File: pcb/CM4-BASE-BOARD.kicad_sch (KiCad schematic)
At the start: 17 parts, among them J1 THD-02-R, J2 Micro_SD_Card_Det2, J3 USB4105-GF-A, J4 PCIe-x1, U1 MagJack-A70-112-331N126, U2 TPD4EUSB30, U3 TPD4EUSB30, U5 RT9742AGJ5F

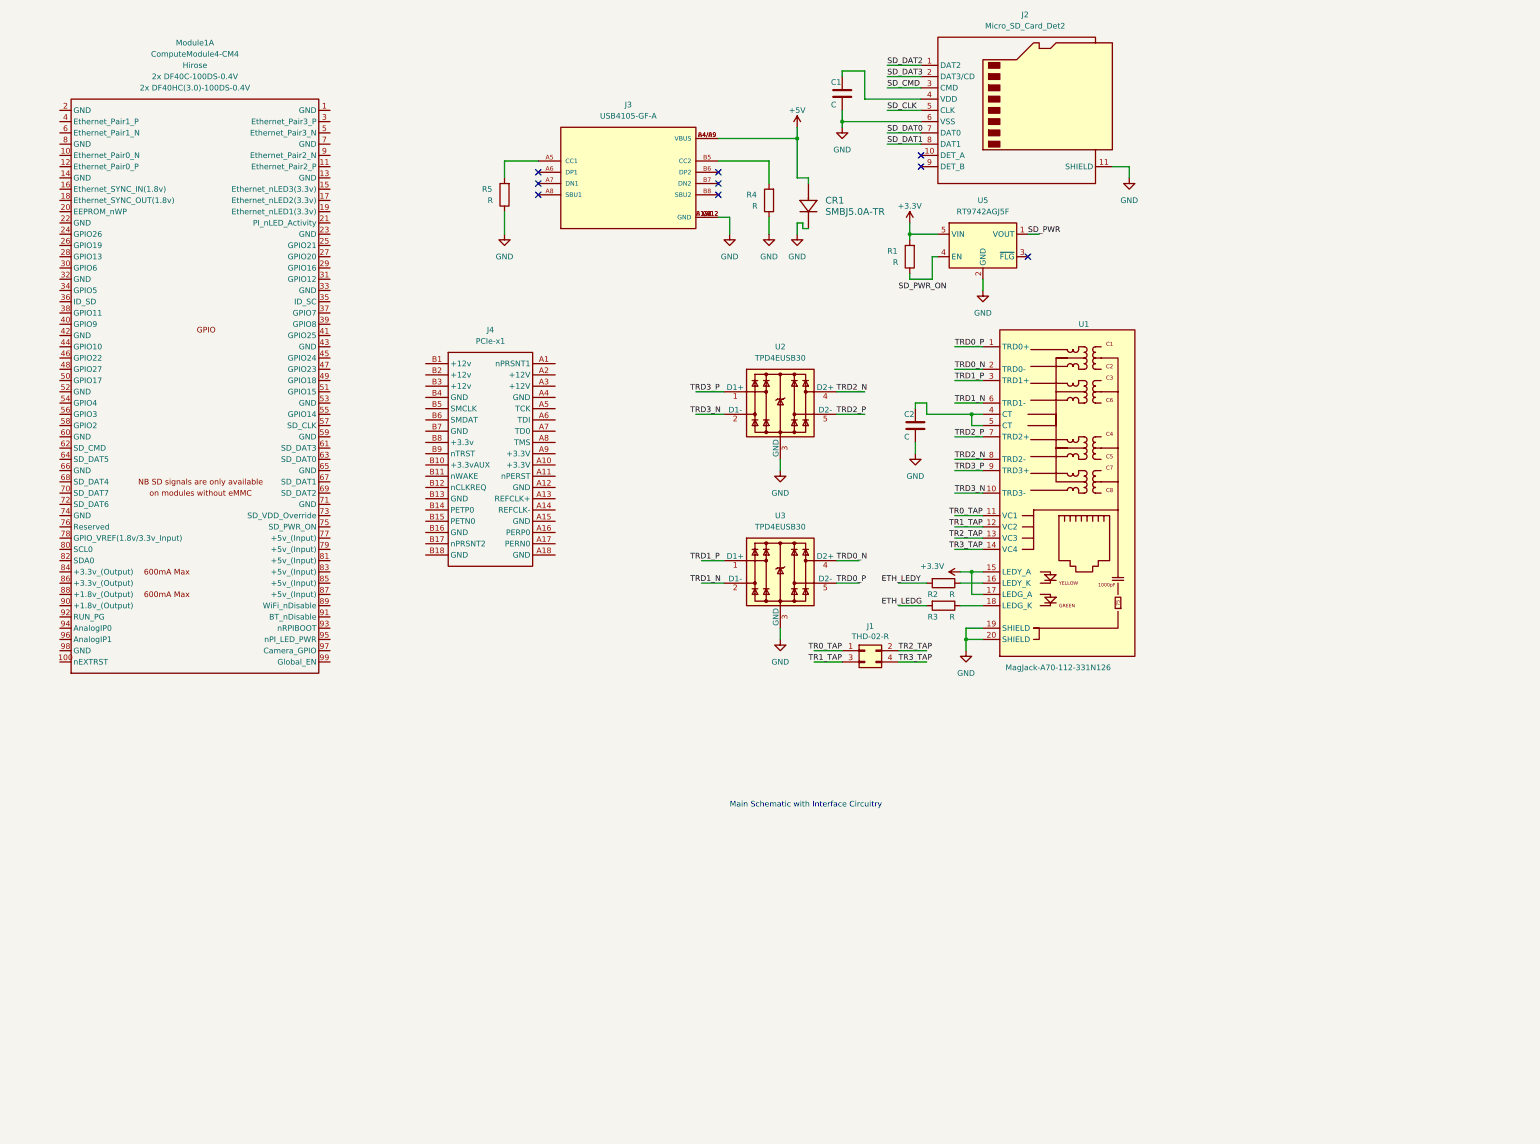
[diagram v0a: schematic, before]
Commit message: Added: concentrator and power section
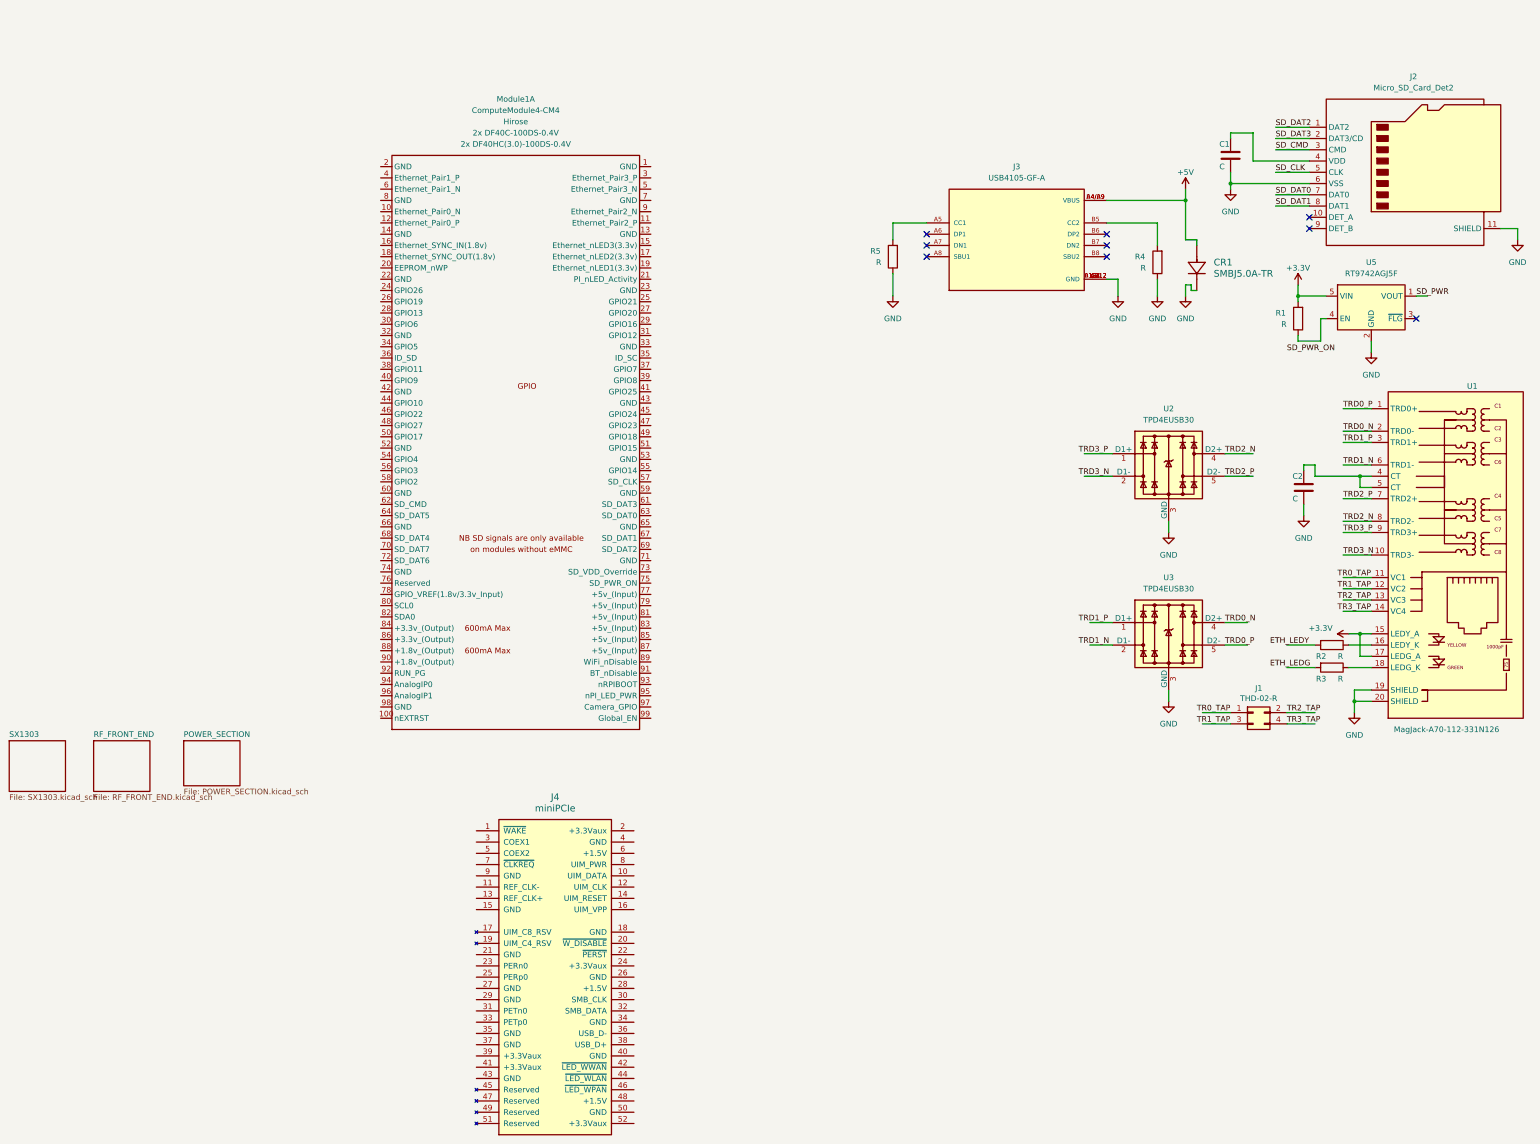
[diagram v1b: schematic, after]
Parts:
- removed J4: PCIe-x1, symbol CM4IO:PCIe-x1
- added J4: miniPCIe, symbol mpcie:miniPCIe
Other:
- added sheet POWER_SECTION (POWER_SECTION.kicad_sch)
- added sheet RF_FRONT_END (RF_FRONT_END.kicad_sch)
- added sheet SX1303 (SX1303.kicad_sch)
- note removed: "Main Schematic with Interface Circuitry"
- moved on the sheet: C1, C2, CR1, J1, J2, J3, Module1A, R1, R2, R3, R4, R5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

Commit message: added:sch
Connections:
- net SD_CLK: now also Module1.57 (SD_CLK)
- net SD_CMD: now also Module1.62 (SD_CMD)
- net SD_DAT0: now also Module1.63 (SD_DAT0)
- net SD_DAT1: now also Module1.67 (SD_DAT1)
- net SD_DAT2: now also Module1.69 (SD_DAT2)
- net SD_DAT3: now also Module1.61 (SD_DAT3)
- net SX1302_GPIO(6): now reaches Module1.27 (GPIO20)
- net HOST_SCK: now reaches Module1.38 (GPIO11)
- net SX1302_CSD: now reaches Module1.39 (GPIO8)
- net HOST_MISO: now reaches Module1.40 (GPIO9)
- net HOST_MOSI: now reaches Module1.44 (GPIO10)
- net SX1302_RESET: now reaches Module1.47 (GPIO23)
- net SX1302_PS_EN: now reaches Module1.49 (GPIO18)
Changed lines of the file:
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@@
+    (stroke (width 0) (type default))
+  )
+  (wire (pts (xy 168.91 106.68) (xy 173.99 106.68))
     (stroke (width 0) (type default))
   )
@@
     (stroke (width 0) (type default))
   )
+  (wire (pts (xy 102.87 99.06) (xy 107.95 99.06))
+    (stroke (width 0) (type default))
+  )
   (wire (pts (xy 325.12 143.51) (xy 331.47 143.51))
     (stroke (width 0) (type default))
@@
     (stroke (width 0) (type default))
   )
+  (wire (pts (xy 168.91 129.54) (xy 180.34 129.54))
+    (stroke (width 0) (type default))
+  )
   (wire (pts (xy 312.42 153.67) (xy 318.77 153.67))
     (stroke (width 0) (type default))
@@
     (stroke (width 0) (type default))
   )
+  (wire (pts (xy 99.06 121.92) (xy 107.95 121.92))
+    (stroke (width 0) (type default))
+  )
   (wire (pts (xy 321.31 80.01) (xy 320.04 80.01))
     (stroke (width 0) (type default))
   )
+  (wire (pts (xy 168.91 124.46) (xy 180.34 124.46))
+    (stroke (width 0) (type default))
+  )
   (wire (pts (xy 325.12 100.33) (xy 331.47 100.33))
     (stroke (width 0) (type default))
@@
     (stroke (width 0) (type default))
   )
+  (wire (pts (xy 102.87 93.98) (xy 107.95 93.98))
+    (stroke (width 0) (type default))
+  )
   (wire (pts (xy 267.97 153.67) (xy 273.05 153.67))
     (stroke (width 0) (type default))
@@
     (stroke (width 0) (type default))
   )
+  (wire (pts (xy 168.91 121.92) (xy 180.34 121.92))
+    (stroke (width 0) (type default))
+  )
   (wire (pts (xy 328.93 156.21) (xy 328.93 151.13))
     (stroke (width 0) (type default))
@@
     (stroke (width 0) (type default))
   )
+  (wire (pts (xy 168.91 116.84) (xy 180.34 116.84))
+    (stroke (width 0) (type default))
+  )
   (wire (pts (xy 328.93 151.13) (xy 331.47 151.13))
     (stroke (width 0) (type default))
   )
+  (wire (pts (xy 168.91 78.74) (xy 173.99 78.74))
+    (stroke (width 0) (type default))
+  )
   (wire (pts (xy 283.21 58.42) (xy 283.21 63.5))
     (stroke (width 0) (type default))
@@
     (stroke (width 0) (type default))
   )
+  (wire (pts (xy 168.91 104.14) (xy 173.99 104.14))
+    (stroke (width 0) (type default))
+  )
   (wire (pts (xy 312.42 168.91) (xy 318.77 168.91))
     (stroke (width 0) (type default))
@@
     (stroke (width 0) (type default))
   )
+  (wire (pts (xy 102.87 91.44) (xy 107.95 91.44))
+    (stroke (width 0) (type default))
+  )
   (wire (pts (xy 271.78 58.42) (xy 283.21 58.42))
     (stroke (width 0) (type default))
@@
     (stroke (width 0) (type default))
   )
+  (wire (pts (xy 168.91 132.08) (xy 180.34 132.08))
+    (stroke (width 0) (type default))
+  )
   (wire (pts (xy 298.45 153.67) (xy 303.53 153.67))
     (stroke (width 0) (type default))
@@
     (stroke (width 0) (type default))
   )
+  (wire (pts (xy 168.91 93.98) (xy 173.99 93.98))
+    (stroke (width 0) (type default))
+  )
   (wire (pts (xy 304.8 38.1) (xy 299.72 38.1))
     (stroke (width 0) (type default))
@@
     (effects (font (size 1.27 1.27)) (justify left bottom))
   )
+  (label "SD_CMD" (at 99.06 121.92 0) (fields_autoplaced)
+    (effects (font (size 1.27 1.27)) (justify left bottom))
+  )
   (label "TRD1_N" (at 325.12 113.03 0) (fields_autoplaced)
     (effects (font (size 1.27 1.27)) (justify left bottom))
@@
     (effects (font (size 1.27 1.27)) (justify left bottom))
   )
+  (label "SD_DAT3" (at 172.72 121.92 0) (fields_autoplaced)
+    (effects (font (size 1.27 1.27)) (justify left bottom))
+  )
   (label "SD_PWR" (at 341.63 74.93 0) (fields_autoplaced)
     (effects (font (size 1.27 1.27)) (justify left bottom))
@@
     (effects (font (size 1.27 1.27)) (justify left bottom))
   )
+  (label "SD_DAT0" (at 172.72 124.46 0) (fields_autoplaced)
+    (effects (font (size 1.27 1.27)) (justify left bottom))
+  )
   (label "TRD3_P" (at 325.12 128.27 0) (fields_autoplaced)
     (effects (font (size 1.27 1.27)) (justify left bottom))
@@
     (effects (font (size 1.27 1.27)) (justify left bottom))
   )
+  (label "SD_DAT1" (at 172.72 129.54 0) (fields_autoplaced)
+    (effects (font (size 1.27 1.27)) (justify left bottom))
+  )
   (label "TR3_TAP" (at 312.42 171.45 0) (fields_autoplaced)
     (effects (font (size 1.27 1.27)) (justify left bottom))
@@
     (effects (font (size 1.27 1.27)) (justify left bottom))
   )
+  (label "SD_DAT2" (at 172.72 132.08 0) (fields_autoplaced)
+    (effects (font (size 1.27 1.27)) (justify left bottom))
+  )
   (label "TR0_TAP" (at 323.85 138.43 0) (fields_autoplaced)
     (effects (font (size 1.27 1.27)) (justify left bottom))
@@
     (effects (font (size 1.27 1.27)) (justify left bottom))
   )
+  (label "SD_CLK" (at 173.99 116.84 0) (fields_autoplaced)
+    (effects (font (size 1.27 1.27)) (justify left bottom))
+  )
   (label "SD_CLK" (at 309.88 46.99 0) (fields_autoplaced)
     (effects (font (size 1.27 1.27)) (justify left bottom))
@@
     (effects (font (size 1.27 1.27)) (justify left bottom))
   )
+  (global_label "HOST_SCK" (shape output) (at 102.87 91.44 180) (fields_autoplaced)
+    (effects (font (size 1.27 1.27)) (justify right))
+    (property "Intersheetrefs" "${INTERSHEET_REFS}" (at 90.409 91.44 0)
+      (effects (font (size 1.27 1.27)) (justify right) hide)
+    )
+  )
+  (global_label "SX1302_RESET" (shape output) (at 173.99 104.14 0) (fields_autoplaced)
+    (effects (font (size 1.27 1.27)) (justify left))
+    (property "Intersheetrefs" "${INTERSHEET_REFS}" (at 190.8655 104.14 0)
+      (effects (font (size 1.27 1.27)) (justify left) hide)
+    )
+  )
+  (global_label "SX1302_GPIO(6)" (shape bidirectional) (at 173.99 78.74 0) (fields_autoplaced)
+    (effects (font (size 1.27 1.27)) (justify left))
+    (property "Intersheetrefs" "${INTERSHEET_REFS}" (at 193.6099 78.74 0)
+      (effects (font (size 1.27 1.27)) (justify left) hide)
+    )
+  )
+  (global_label "HOST_MOSI" (shape output) (at 102.87 99.06 180) (fields_autoplaced)
+    (effects (font (size 1.27 1.27)) (justify right))
+    (property "Intersheetrefs" "${INTERSHEET_REFS}" (at 89.5623 99.06 0)
+      (effects (font (size 1.27 1.27)) (justify right) hide)
+    )
+  )
+  (global_label "SX1302_PS_EN" (shape output) (at 173.99 106.68 0) (fields_autoplaced)
+    (effects (font (size 1.27 1.27)) (justify left))
+    (property "Intersheetrefs" "${INTERSHEET_REFS}" (at 191.047 106.68 0)
+      (effects (font (size 1.27 1.27)) (justify left) hide)
+    )
+  )
+  (global_label "HOST_MISO" (shape input) (at 102.87 93.98 180) (fields_autoplaced)
+    (effects (font (size 1.27 1.27)) (justify right))
+    (property "Intersheetrefs" "${INTERSHEET_REFS}" (at 89.5623 93.98 0)
+      (effects (font (size 1.27 1.27)) (justify right) hide)
+    )
+  )
+  (global_label "SX1302_CSD" (shape input) (at 173.99 93.98 0) (fields_autoplaced)
+    (effects (font (size 1.27 1.27)) (justify left))
+    (property "Intersheetrefs" "${INTERSHEET_REFS}" (at 188.8699 93.98 0)
+      (effects (font (size 1.27 1.27)) (justify left) hide)
+    )
+  )
   (symbol (lib_id "power:GND") (at 364.49 62.23 0) (unit 1)
